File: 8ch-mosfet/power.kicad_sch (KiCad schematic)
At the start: 21 parts, among them J3 Screw_Terminal_01x08, J4 Screw_Terminal_01x08, U4 XL1509-5.0

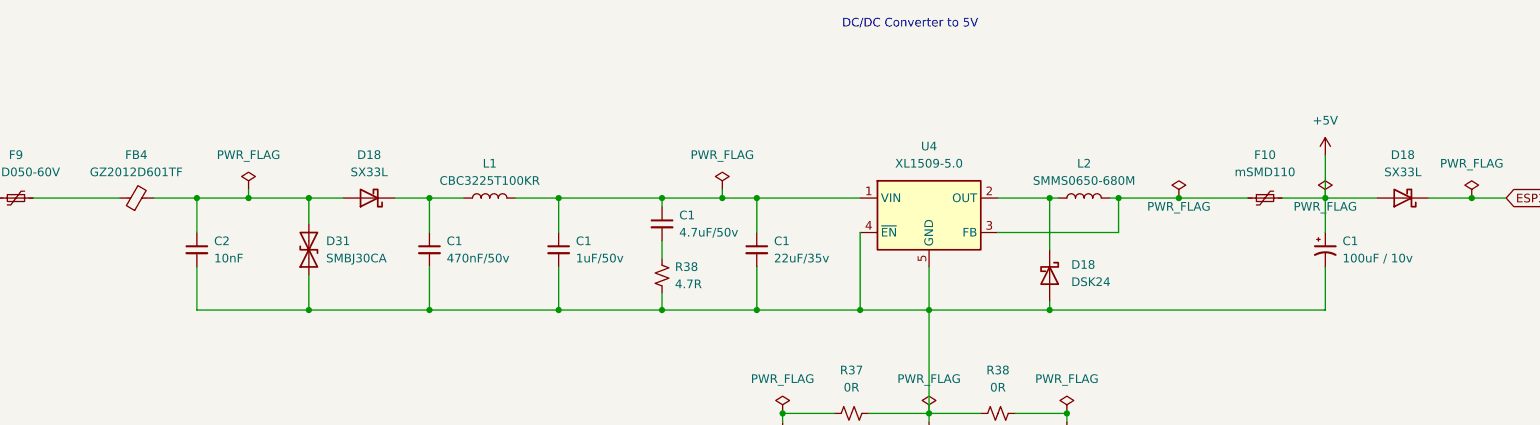
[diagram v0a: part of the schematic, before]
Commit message: changed to MCP3564
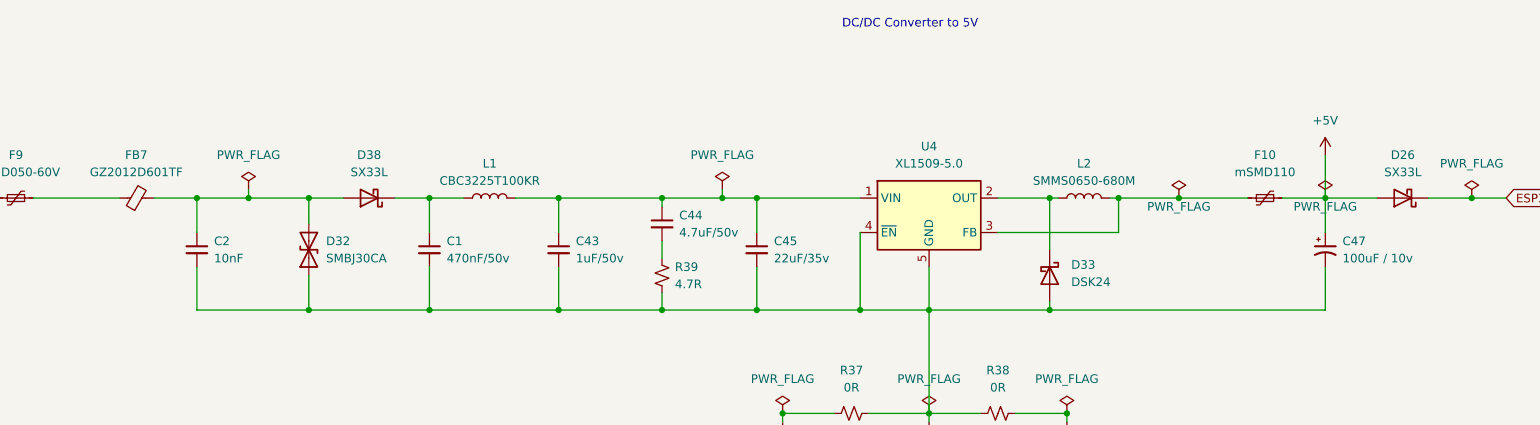
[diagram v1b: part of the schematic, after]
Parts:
- F9: value mSMD050-60V -> mSMD050-60V
- renumbered C1 to C43, C1 to C44, C1 to C45, C1 to C47, D18 to D26, D31 to D32, D18 to D33, D18 to D38, FB4 to FB7, R38 to R39

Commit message: updated busbar design.
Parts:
- J3, J4: footprint yarrboard:Busbar 1x9 .375in -> yarrboard:Busbar Rev D
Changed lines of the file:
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@@
 			)
 		)
-		(property "Footprint" "yarrboard:Busbar 1x9 .375in"
+		(property "Footprint" "yarrboard:Busbar Rev D"
 			(at 40.64 144.78 0)
 			(effects
@@
 			)
 		)
-		(property "Footprint" "yarrboard:Busbar 1x9 .375in"
+		(property "Footprint" "yarrboard:Busbar Rev D"
 			(at 62.23 144.78 0)
 			(effects

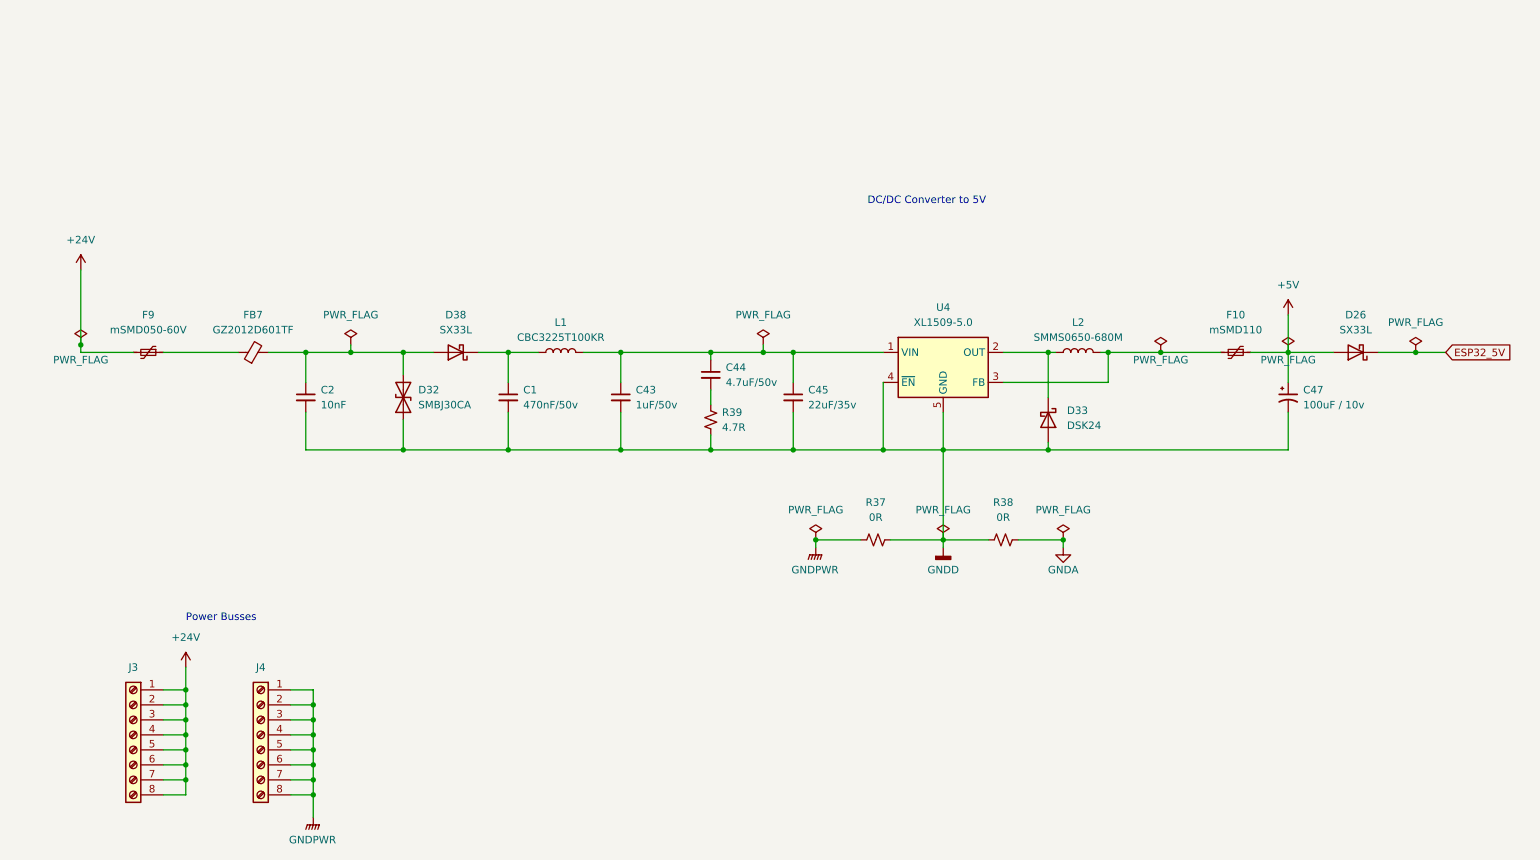
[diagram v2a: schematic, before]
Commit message: big update - 12ch, volt adc, senders, etc.
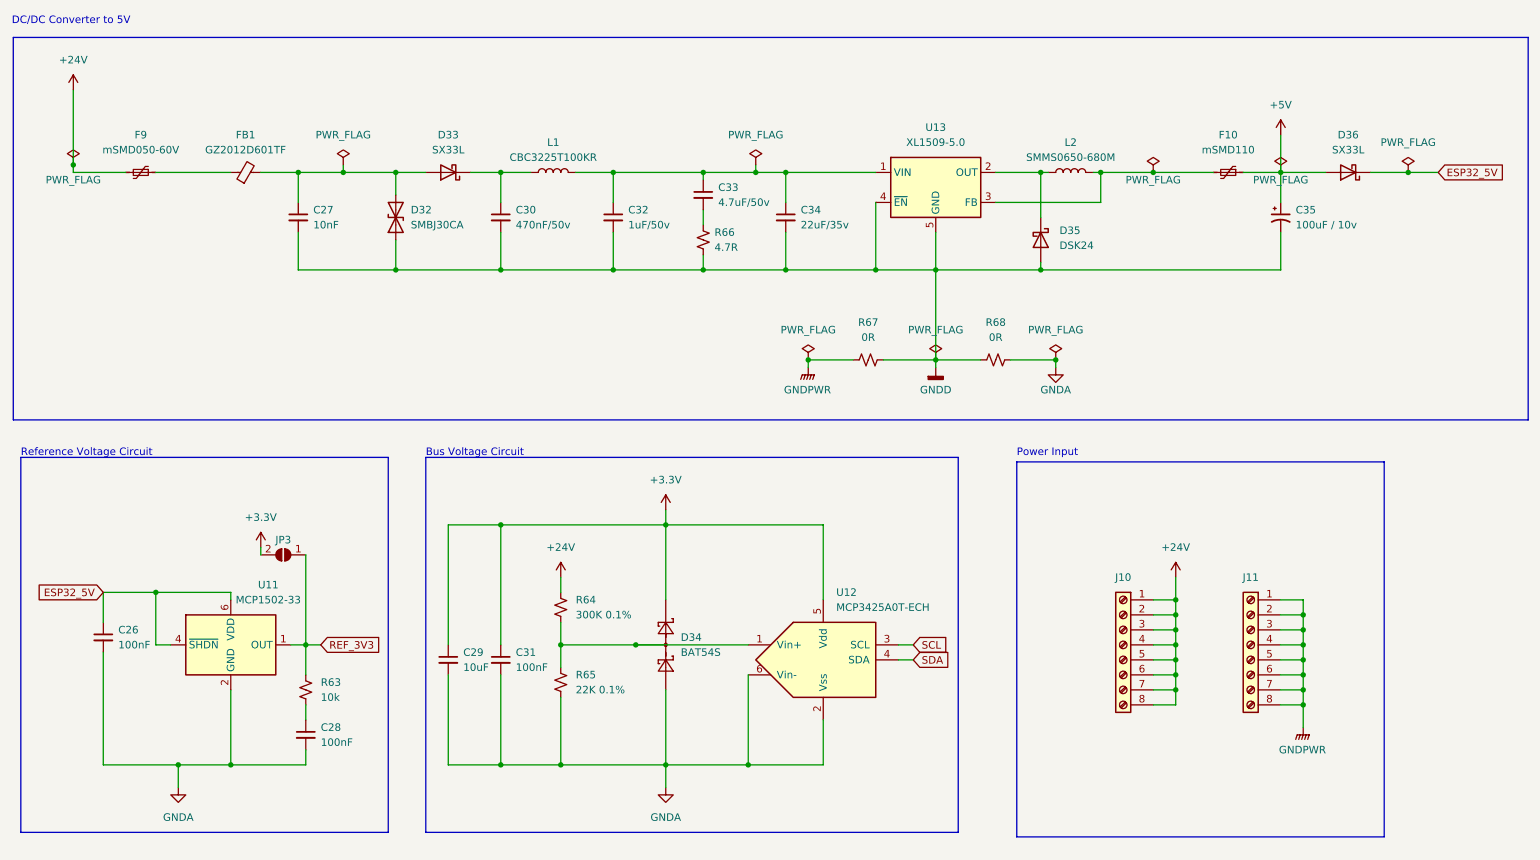
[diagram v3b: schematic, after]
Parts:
- added C26, C28, C31: 100nF, Capacitor_SMD:C_0805_2012Metric_Pad1.18x1.45mm_HandSolder, symbol Device:C_Small
- added C29: 10uF, Capacitor_SMD:C_0805_2012Metric_Pad1.18x1.45mm_HandSolder, symbol Device:C_Small
- added D34: BAT54S, Package_TO_SOT_SMD:SOT-23, symbol Diode:BAT54S
- added JP3: SolderJumper_2_Open, Jumper:SolderJumper-2_P1.3mm_Open_RoundedPad1.0x1.5mm, symbol Jumper:SolderJumper_2_Open
- added R63: 10k, Resistor_SMD:R_0805_2012Metric_Pad1.20x1.40mm_HandSolder, symbol Device:R_Small_US
- added R64: 300K 0.1%, Resistor_SMD:R_0805_2012Metric_Pad1.20x1.40mm_HandSolder, symbol Device:R_Small_US
- added R65: 22K 0.1%, Resistor_SMD:R_0805_2012Metric_Pad1.20x1.40mm_HandSolder, symbol Device:R_Small_US
- added U11: MCP1502-33, Package_TO_SOT_SMD:SOT-23-6, symbol Reference_Voltage:MCP1501-30xCH
- added U12: MCP3425A0T-ECH, Package_TO_SOT_SMD:SOT-23-6, symbol Analog_ADC:MCP3425A0T-ECH
- renumbered C2 to C27, C1 to C30, C43 to C32, C44 to C33, C45 to C34, C47 to C35, D38 to D33, D33 to D35, D26 to D36, FB7 to FB1, J3 to J10, J4 to J11, R39 to R66, R37 to R67, R38 to R68, U4 to U13
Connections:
- net +24V: now also R64.2
- net ESP32_5V: now also C26.1, U11.4 (~{SHDN}), U11.6 (VDD)
- net GNDA: now also C26.2, C28.2, C29.2, C31.2, D34.1 (A), R65.1, U11.2 (GND), U11.3 (GND), U11.5 (GND), U12.2 (Vss), U12.6 (Vin-)
- new net: D34.3 (COM), R64.1, R65.2, U12.1 (Vin+)
- new net: C28.1, R63.1
- new net +3.3V: C29.1, C31.1, D34.2 (K), JP3.2 (B), U12.5 (Vdd)
- new net REF_3V3: JP3.1 (A), R63.2, U11.1 (OUT)
- new net SCL: U12.3 (SCL)
- new net SDA: U12.4 (SDA)
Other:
- note added: "Bus Voltage Circuit"
- note added: "Power Input"
- note added: "Reference Voltage Circuit"
- note removed: "Power Busses"
- moved on the sheet: C27, C30, C32, C33, C34, C35, D32, D33, D35, D36, F10, F9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

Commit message: component layout looking crispy.
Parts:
- removed J10, J11: Screw_Terminal_01x08, yarrboard:Busbar Rev D, symbol Connector:Screw_Terminal_01x08
- added J10, J9: Screw_Terminal_01x12, yarrboard:Busbar Rev D, symbol Connector:Screw_Terminal_01x12
- R67, R68: now not fitted
- renumbered D32 to D29, D33 to D30, D34 to D31, D35 to D32, D36 to D33
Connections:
- net GNDD is gone; now on net GNDA: C27.2, C30.2, C32.2, C34.2, C35.2, D29.1 (A1), D32.2 (A), R66.2, R67.1, R68.2, U13.4 (~{EN}), U13.5 (GND), U13.6 (GND), U13.7 (GND), U13.8 (GND)
- net GNDPWR is gone; now on net GNDA: R67.2
- net +24V: now also J9.1 (Pin_1), J9.10 (Pin_10), J9.11 (Pin_11), J9.12 (Pin_12), J9.2 (Pin_2), J9.3 (Pin_3), J9.4 (Pin_4), J9.5 (Pin_5), J9.6 (Pin_6), J9.7 (Pin_7), J9.8 (Pin_8), J9.9 (Pin_9)
- net GNDA: now also J10.1 (Pin_1), J10.10 (Pin_10), J10.11 (Pin_11), J10.12 (Pin_12), J10.2 (Pin_2), J10.3 (Pin_3), J10.4 (Pin_4), J10.5 (Pin_5), J10.6 (Pin_6), J10.7 (Pin_7), J10.8 (Pin_8), J10.9 (Pin_9)
